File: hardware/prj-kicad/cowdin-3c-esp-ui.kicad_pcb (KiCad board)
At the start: 2 copper layers, 49 x 42 mm, 18 parts, among them P1 CONN_F52R-04, SW1 SW_PUSH, SW2 SW_PUSH, SW3 SW_PUSH, SW4 SW_PUSH, SW5 SW_PUSH

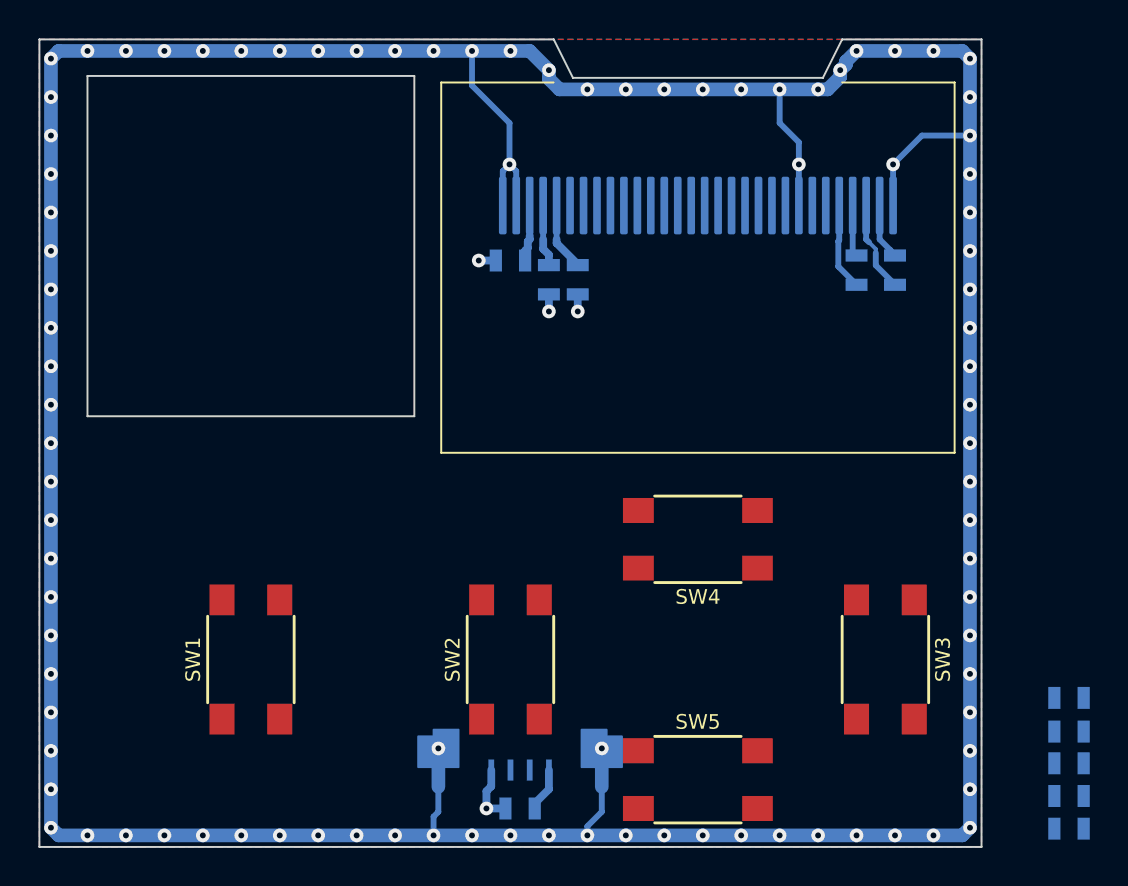
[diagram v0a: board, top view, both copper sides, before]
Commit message: Hardware: Add MCU and main components. Create productions files for rev1
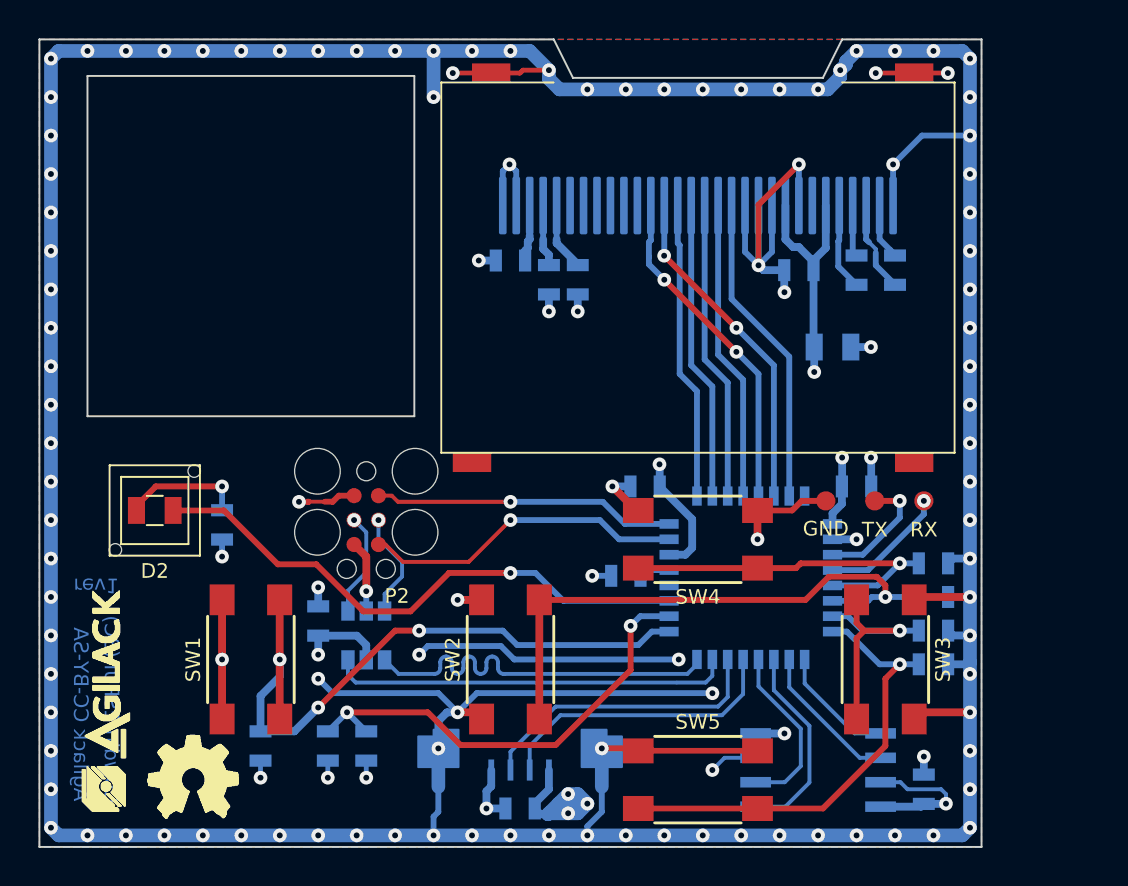
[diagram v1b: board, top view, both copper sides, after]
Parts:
- added C11: 1uF, cowdin-3c-esp-ui:SMD0603, B.Cu at (138.5, 114.2)
- added C12: 1uF, cowdin-3c-esp-ui:SMD0603, B.Cu at (154.5, 111.9)
- added C13: 1uF, cowdin-3c-esp-ui:SMD0603, B.Cu at (139.0, 120.8)
- added C14: 100nF, cowdin-3c-esp-ui:SMD0603, B.Cu at (155.5, 107.2)
- added C15: 100nF, cowdin-3c-esp-ui:SMD0603, B.Cu at (166.5, 107.2)
- added C16: 4,7uF, cowdin-3c-esp-ui:SMD0805, B.Cu at (165.2, 100.0)
- added C17: 100nF, cowdin-3c-esp-ui:SMD0603, B.Cu at (163.5, 96.0)
- added C18: 100nF, cowdin-3c-esp-ui:SMD0603, B.Cu at (170.0, 123.0)
- added D1: USBLC6-2, cowdin-3c-esp-ui:SOT23-6, B.Cu at (141.0, 115.0)
- added D2: LED, cowdin-3c-esp-ui:SMD0805, F.Cu at (130.0, 108.5)
- added P2: CONN_TC2030, cowdin-3c-esp-ui:TC2030-MCP-FP, F.Cu at (141.0, 109.0)
- added R2: 10k, cowdin-3c-esp-ui:SMD0603, B.Cu at (141.0, 120.8)
- added R3: 330, cowdin-3c-esp-ui:SMD0603, B.Cu at (133.5, 109.2)
- added REF**: LED-PIPE, cowdin-3c-esp-ui:LED-PIPE, F.Cu at (130.0, 108.5)
- added SHLD1: CONN_1, cowdin-3c-esp-ui:SHLD_PAD, F.Cu at (147.5, 85.8)
- added SHLD2: CONN_1, cowdin-3c-esp-ui:SHLD_PAD, F.Cu at (169.5, 85.8)
- added SHLD3: CONN_1, cowdin-3c-esp-ui:SHLD_PAD, F.Cu at (169.5, 106.0)
- added SHLD4: CONN_1, cowdin-3c-esp-ui:SHLD_PAD, F.Cu at (146.5, 106.0)
- added TP1: CONN_1, cowdin-3c-esp-ui:TP_SMD, F.Cu at (167.4, 108.0)
- added TP2: CONN_1, cowdin-3c-esp-ui:TP_SMD, F.Cu at (170.0, 108.0)
- added TP3: CONN_1, cowdin-3c-esp-ui:TP_SMD, F.Cu at (164.9, 108.0)
- added U1: ATSAMD21Exx, cowdin-3c-esp-ui:TQFP32, B.Cu at (161.0, 112.0)
- added U2: W25Q16JV, cowdin-3c-esp-ui:SOIC-8, B.Cu at (164.5, 122.0)
- added agilack-11.5: 450px, cowdin-3c-esp-ui:logo-agilack-11.5, F.Cu at (127.5, 118.0)
- added ohw_logo: VAL**, cowdin-3c-esp-ui:logo-ohw, F.Cu at (132.0, 122.5)
- moved C2 42.1 mm to (135.5, 120.8), turned to -90 degrees
- moved C5 14.0 mm to (170.5, 111.2)
- moved C6 11.1 mm to (170.5, 116.5)
- moved C3 9.93 mm to (170.5, 113.0)
- moved C4 9.86 mm to (170.5, 114.8)
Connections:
- DISP1 pad 10: unconnected-(DISP1-Pad10) -> GND
- DISP1 pad 11: unconnected-(DISP1-Pad11) -> GND
- DISP1 pad 12: unconnected-(DISP1-Pad12) -> GND
- DISP1 pad 13: unconnected-(DISP1-Pad13) -> DISP_SCS
- DISP1 pad 14: unconnected-(DISP1-Pad14) -> DISP_RST
- DISP1 pad 15: unconnected-(DISP1-Pad15) -> DISP_DC
- DISP1 pad 16: unconnected-(DISP1-Pad16) -> DISP_RW
- DISP1 pad 17: unconnected-(DISP1-Pad17) -> DISP_ERD
- DISP1 pad 18: unconnected-(DISP1-Pad18) -> DISP_SCK
- DISP1 pad 19: unconnected-(DISP1-Pad19) -> DISP_MOSI
- DISP1 pad 6: unconnected-(DISP1-Pad6) -> +3.3V
- DISP1 pad 9: unconnected-(DISP1-Pad9) -> +3.3V
- P1 pad 2: unconnected-(P1-Pad2) -> UART_RX
- P1 pad 3: unconnected-(P1-Pad3) -> UART_TX
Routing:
- net GND: track 218.2 -> 438.1 mm, vias 98 -> 123
- net +3.3V: track 2.31 -> 128.6 mm, vias 0 -> 10
- net SW1: track 0.00 -> 34.4 mm, vias 0 -> 3
- net SW2: track 0.00 -> 30.1 mm, vias 0 -> 1
- net LED1: track 0.00 -> 29.4 mm, vias 0 -> 1
- net RST: track 0.00 -> 24.4 mm, vias 0 -> 2
- net SW5: track 0.00 -> 23.9 mm, vias 0 -> 1
- net USB_D-: track 0.00 -> 20.9 mm
- net USB_D+: track 0.00 -> 20.7 mm
- net SW4: track 0.00 -> 18.7 mm, vias 0 -> 1
- net DISP_MOSI: track 0.00 -> 17.5 mm, vias 0 -> 2
- net DISP_SCK: track 0.00 -> 17.5 mm, vias 0 -> 2
- net SWCLK: track 0.00 -> 16.8 mm, vias 0 -> 1
- net +VUSB: track 0.00 -> 16.7 mm, vias 0 -> 2
- net DISP_SCS: track 0.00 -> 16.4 mm
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- added copper zone on In2.Cu, net +3.3V
- added copper zone on In1.Cu, net GND
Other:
- copper layers 2 -> 4
- board text added: "Agilack CC-BY-SA"
- board text added: "Cowdin-ESPUI (3C)"
- board text added: "GND"
- board text added: "RX"
- board text added: "TX"
- board text added: "rev1"
- board text removed: "CowDIN"
